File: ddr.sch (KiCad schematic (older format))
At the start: 2 parts

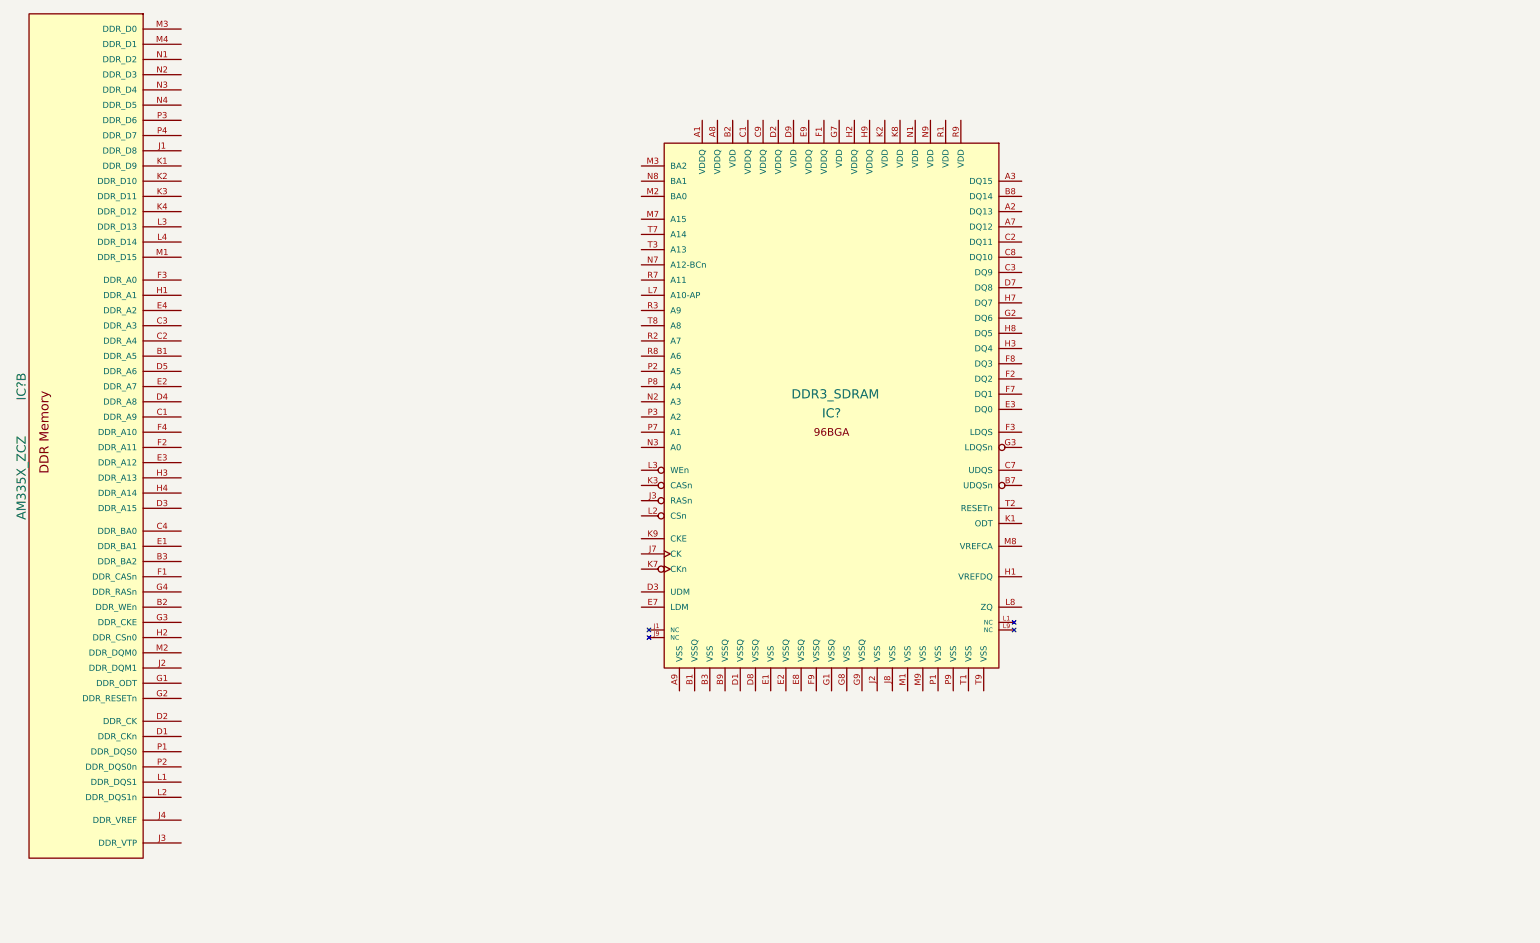
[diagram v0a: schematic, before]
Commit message: emmc nand and micro sd
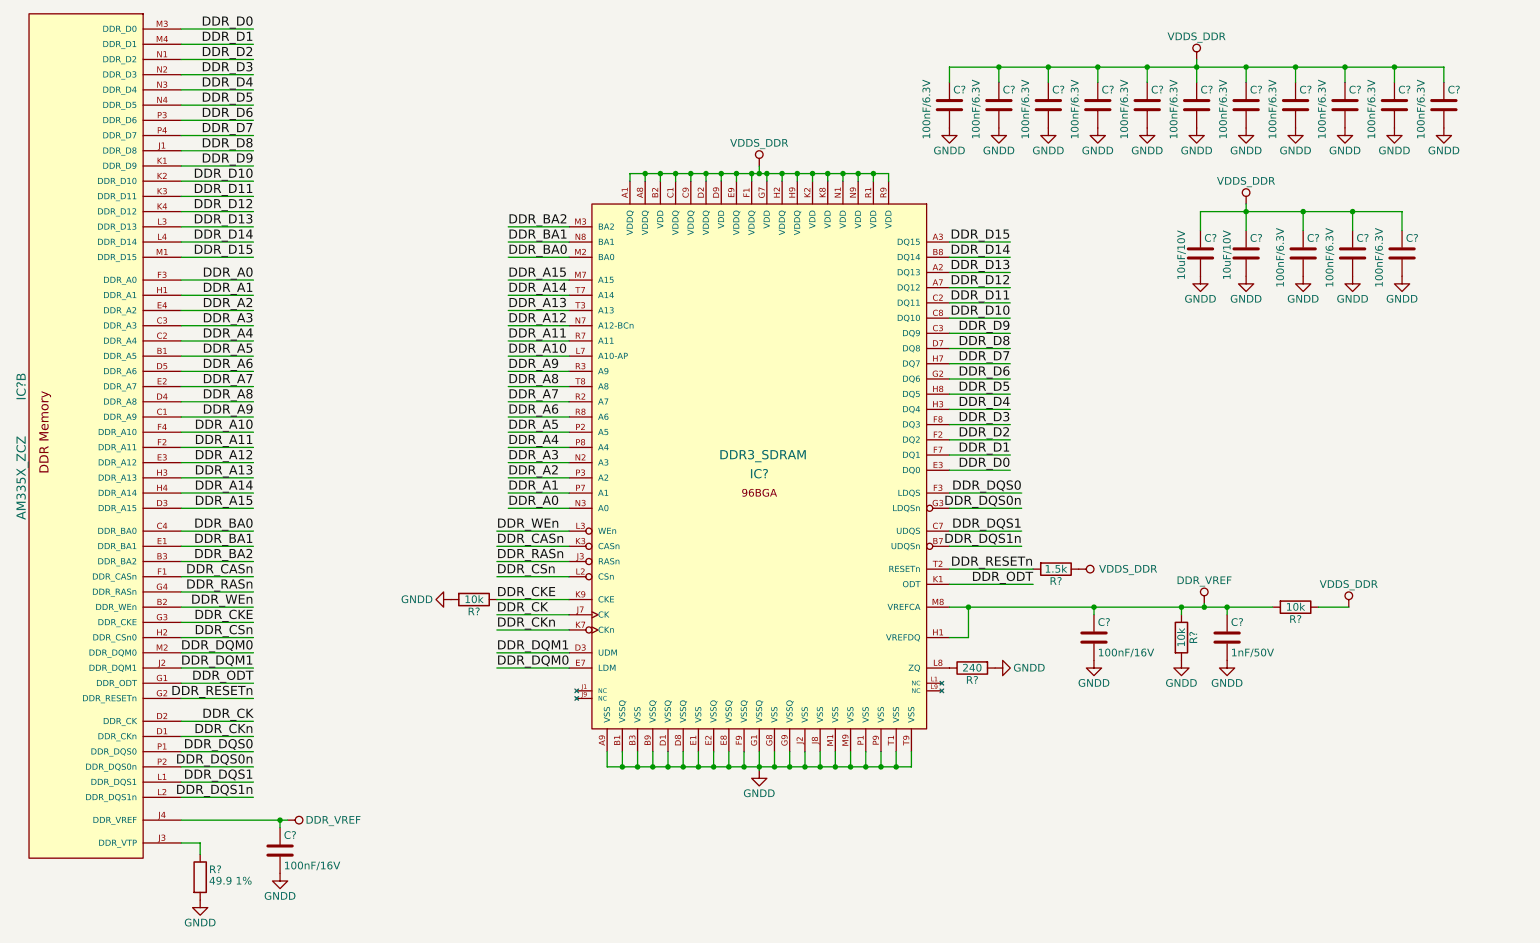
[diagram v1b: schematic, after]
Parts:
- added C?: 1nF/50V, symbol C
- added C? (x14): 100nF/6.3V, symbol C
- added C? (x2): 100nF/16V, symbol C
- added C? (x2): 10uF/10V, symbol C
- added R? (x3): 10k, symbol R
- added R?: 49.9 1%, symbol R
- added R?: 1.5k, symbol R
- added R?: 240, symbol R
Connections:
- net DDR_A5: now reaches IC?.B1 (DDR_A5)
- net DDR_A5: now also IC?.P2 (A5)
- net DDR_WEn: now reaches IC?.B2 (DDR_WEn)
- net DDR_WEn: now also IC?.L3 (WEn)
- net DDR_BA2: now reaches IC?.B3 (DDR_BA2)
- net DDR_BA2: now also IC?.M3 (BA2)
- net DDR_A9: now reaches IC?.C1 (DDR_A9)
- net DDR_A9: now also IC?.R3 (A9)
- net DDR_A4: now reaches IC?.C2 (DDR_A4)
- net DDR_A4: now also IC?.P8 (A4)
- net DDR_A3: now reaches IC?.C3 (DDR_A3)
- net DDR_A3: now also IC?.N2 (A3)
- net DDR_BA0: now reaches IC?.C4 (DDR_BA0)
- net DDR_BA0: now also IC?.M2 (BA0)
- net DDR_CKn: now reaches IC?.D1 (DDR_CKn)
- net DDR_CKn: now also IC?.K7 (CKn)
- net DDR_CK: now reaches IC?.D2 (DDR_CK)
- net DDR_CK: now also IC?.J7 (CK)
- net DDR_A15: now reaches IC?.D3 (DDR_A15)
- net DDR_A15: now also IC?.M7 (A15)
- net DDR_A8: now reaches IC?.D4 (DDR_A8)
- net DDR_A8: now also IC?.T8 (A8)
- net DDR_A6: now reaches IC?.D5 (DDR_A6)
- net DDR_A6: now also IC?.R8 (A6)
- net DDR_BA1: now reaches IC?.E1 (DDR_BA1)
- net DDR_BA1: now also IC?.N8 (BA1)
- net DDR_A7: now reaches IC?.E2 (DDR_A7)
- net DDR_A7: now also IC?.R2 (A7)
- net DDR_A12: now reaches IC?.E3 (DDR_A12)
- net DDR_A12: now also IC?.N7 (A12-BCn)
- net DDR_A2: now reaches IC?.E4 (DDR_A2)
- net DDR_A2: now also IC?.P3 (A2)
- net DDR_CASn: now reaches IC?.F1 (DDR_CASn)
- net DDR_CASn: now also IC?.K3 (CASn)
- net DDR_A11: now reaches IC?.F2 (DDR_A11)
- net DDR_A11: now also IC?.R7 (A11)
- net DDR_A0: now reaches IC?.F3 (DDR_A0)
- net DDR_A0: now also IC?.N3 (A0)
- net DDR_A10: now reaches IC?.F4 (DDR_A10)
- net DDR_A10: now also IC?.L7 (A10-AP)
- net DDR_ODT: now reaches IC?.G1 (DDR_ODT)
- net DDR_ODT: now also IC?.K1 (ODT)
- net DDR_RESETn: now reaches IC?.G2 (DDR_RESETn)
- net DDR_RESETn: now also IC?.T2 (RESETn), R?.2
- net DDR_CKE: now reaches IC?.G3 (DDR_CKE)
- net DDR_CKE: now also IC?.K9 (CKE), R?.1
- net DDR_RASn: now reaches IC?.G4 (DDR_RASn)
- net DDR_RASn: now also IC?.J3 (RASn)
- net DDR_A1: now reaches IC?.H1 (DDR_A1)
- net DDR_A1: now also IC?.P7 (A1)
- net DDR_CSn: now reaches IC?.H2 (DDR_CSn0)
- net DDR_CSn: now also IC?.L2 (CSn)
- net DDR_A13: now reaches IC?.H3 (DDR_A13)
- net DDR_A13: now also IC?.T3 (A13)
- net DDR_A14: now reaches IC?.H4 (DDR_A14)
- net DDR_A14: now also IC?.T7 (A14)
- net DDR_D8: now reaches IC?.J1 (DDR_D8)
- net DDR_D8: now also IC?.D7 (DQ8)
- net DDR_DQM1: now reaches IC?.J2 (DDR_DQM1)
- net DDR_DQM1: now also IC?.D3 (UDM)
- net at IC?.J3 (DDR_VTP): now also R?.1
- net DDR_VREF: now reaches IC?.J4 (DDR_VREF)
- net DDR_VREF: now also IC?.H1 (VREFDQ), IC?.M8 (VREFCA), C?.1, C?.1, C?.1, R?.1, R?.2
- net DDR_D9: now reaches IC?.K1 (DDR_D9)
- net DDR_D9: now also IC?.C3 (DQ9)
- net DDR_D10: now reaches IC?.K2 (DDR_D10)
- net DDR_D10: now also IC?.C8 (DQ10)
- net DDR_D11: now reaches IC?.K3 (DDR_D11)
- net DDR_D11: now also IC?.C2 (DQ11)
- net DDR_D12: now reaches IC?.K4 (DDR_D12)
- net DDR_D12: now also IC?.A7 (DQ12)
- net DDR_DQS1: now reaches IC?.L1 (DDR_DQS1)
- net DDR_DQS1: now also IC?.C7 (UDQS)
- net DDR_DQS1n: now reaches IC?.L2 (DDR_DQS1n)
- net DDR_DQS1n: now also IC?.B7 (UDQSn)
- net DDR_D13: now reaches IC?.L3 (DDR_D13)
- net DDR_D13: now also IC?.A2 (DQ13)
- net DDR_D14: now reaches IC?.L4 (DDR_D14)
- net DDR_D14: now also IC?.B8 (DQ14)
- net DDR_D15: now reaches IC?.M1 (DDR_D15)
- net DDR_D15: now also IC?.A3 (DQ15)
- net DDR_DQM0: now reaches IC?.M2 (DDR_DQM0)
- net DDR_DQM0: now also IC?.E7 (LDM)
- net DDR_D0: now reaches IC?.M3 (DDR_D0)
- net DDR_D0: now also IC?.E3 (DQ0)
- net DDR_D1: now reaches IC?.M4 (DDR_D1)
- net DDR_D1: now also IC?.F7 (DQ1)
- net DDR_D2: now reaches IC?.N1 (DDR_D2)
- net DDR_D2: now also IC?.F2 (DQ2)
- net DDR_D3: now reaches IC?.N2 (DDR_D3)
- net DDR_D3: now also IC?.F8 (DQ3)
- net DDR_D4: now reaches IC?.N3 (DDR_D4)
- net DDR_D4: now also IC?.H3 (DQ4)
- net DDR_D5: now reaches IC?.N4 (DDR_D5)
- net DDR_D5: now also IC?.H8 (DQ5)
- net DDR_DQS0: now reaches IC?.P1 (DDR_DQS0)
- net DDR_DQS0: now also IC?.F3 (LDQS)
- net DDR_DQS0n: now reaches IC?.P2 (DDR_DQS0n)
- net DDR_DQS0n: now also IC?.G3 (LDQSn)
- net DDR_D6: now reaches IC?.P3 (DDR_D6)
- net DDR_D6: now also IC?.G2 (DQ6)
- net DDR_D7: now reaches IC?.P4 (DDR_D7)
- net DDR_D7: now also IC?.H7 (DQ7)
- net VDDS_DDR: now reaches IC?.A1 (VDDQ)
- net VDDS_DDR: now also IC?.A8 (VDDQ), IC?.B2 (VDD), IC?.C1 (VDDQ), IC?.C9 (VDDQ), IC?.D2 (VDDQ), IC?.D9 (VDD), IC?.E9 (VDDQ), IC?.F1 (VDDQ), IC?.G7 (VDD), IC?.H2 (VDDQ), IC?.H9 (VDDQ), IC?.K2 (VDD), IC?.K8 (VDD), IC?.N1 (VDD), IC?.N9 (VDD), IC?.R1 (VDD), IC?.R9 (VDD), C?.1, C?.1, C?.1, C?.1, C?.1, C?.1, C?.1, C?.1, C?.1, C?.1, C?.1, C?.1, C?.1, C?.1, C?.1, C?.1, R?.1, R?.1
- net GNDD: now reaches IC?.A9 (VSS)
- net GNDD: now also IC?.B1 (VSSQ), IC?.B3 (VSS), IC?.B9 (VSSQ), IC?.D1 (VSSQ), IC?.D8 (VSSQ), IC?.E1 (VSS), IC?.E2 (VSSQ), IC?.E8 (VSSQ), IC?.F9 (VSSQ), IC?.G1 (VSSQ), IC?.G8 (VSS), IC?.G9 (VSSQ), IC?.J2 (VSS), IC?.J8 (VSS), IC?.M1 (VSS), IC?.M9 (VSS), IC?.P1 (VSS), IC?.P9 (VSS), IC?.T1 (VSS), IC?.T9 (VSS), C?.2, C?.2, C?.2, C?.2, C?.2, C?.2, C?.2, C?.2, C?.2, C?.2, C?.2, C?.2, C?.2, C?.2, C?.2, C?.2, C?.2, C?.2, C?.2, R?.2, R?.2, R?.2, R?.2
- net at IC?.L8 (ZQ): now also R?.1
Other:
- moved on the sheet: IC?

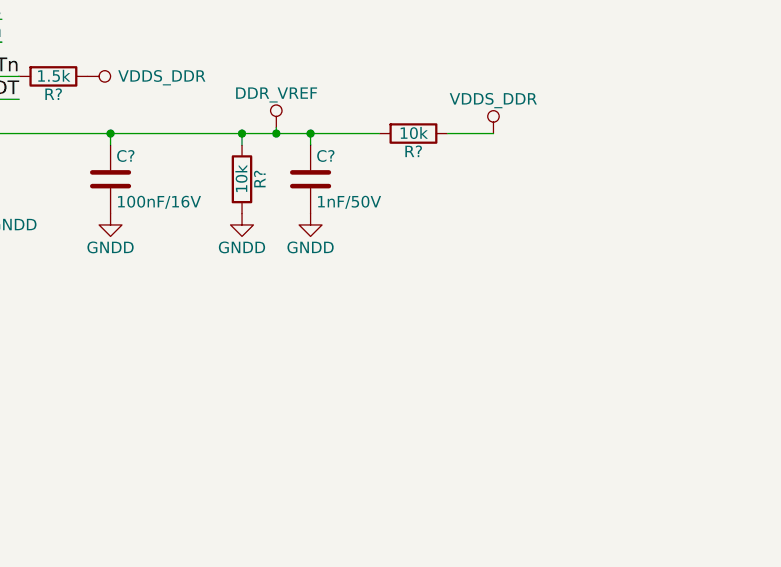
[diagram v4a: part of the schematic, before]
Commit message: wip wl1835 lib
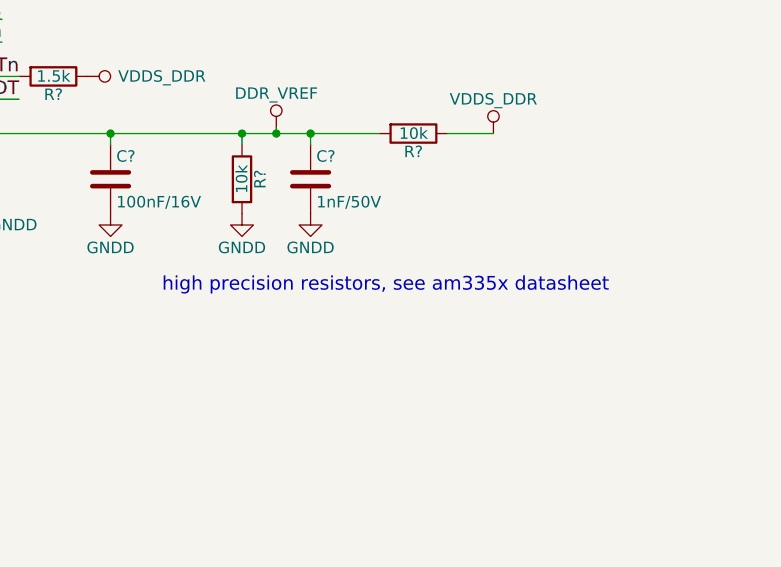
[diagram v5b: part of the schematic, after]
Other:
- note added: "high precision resistors, see am335x datasheet"
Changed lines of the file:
@@
 EESchema Schematic File Version 2
+LIBS:mateboard-rescue
 LIBS:power
 LIBS:device
@@
 	1    0    0    -1
 $EndComp
+Text Notes 8325 5350 0    60   ~ 0
+high precision resistors, see am335x datasheet
 $EndSCHEMATC

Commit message: annotation, wip erc
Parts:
- gave numbers to parts that had none: 27
